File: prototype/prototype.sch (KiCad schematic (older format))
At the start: 2 parts

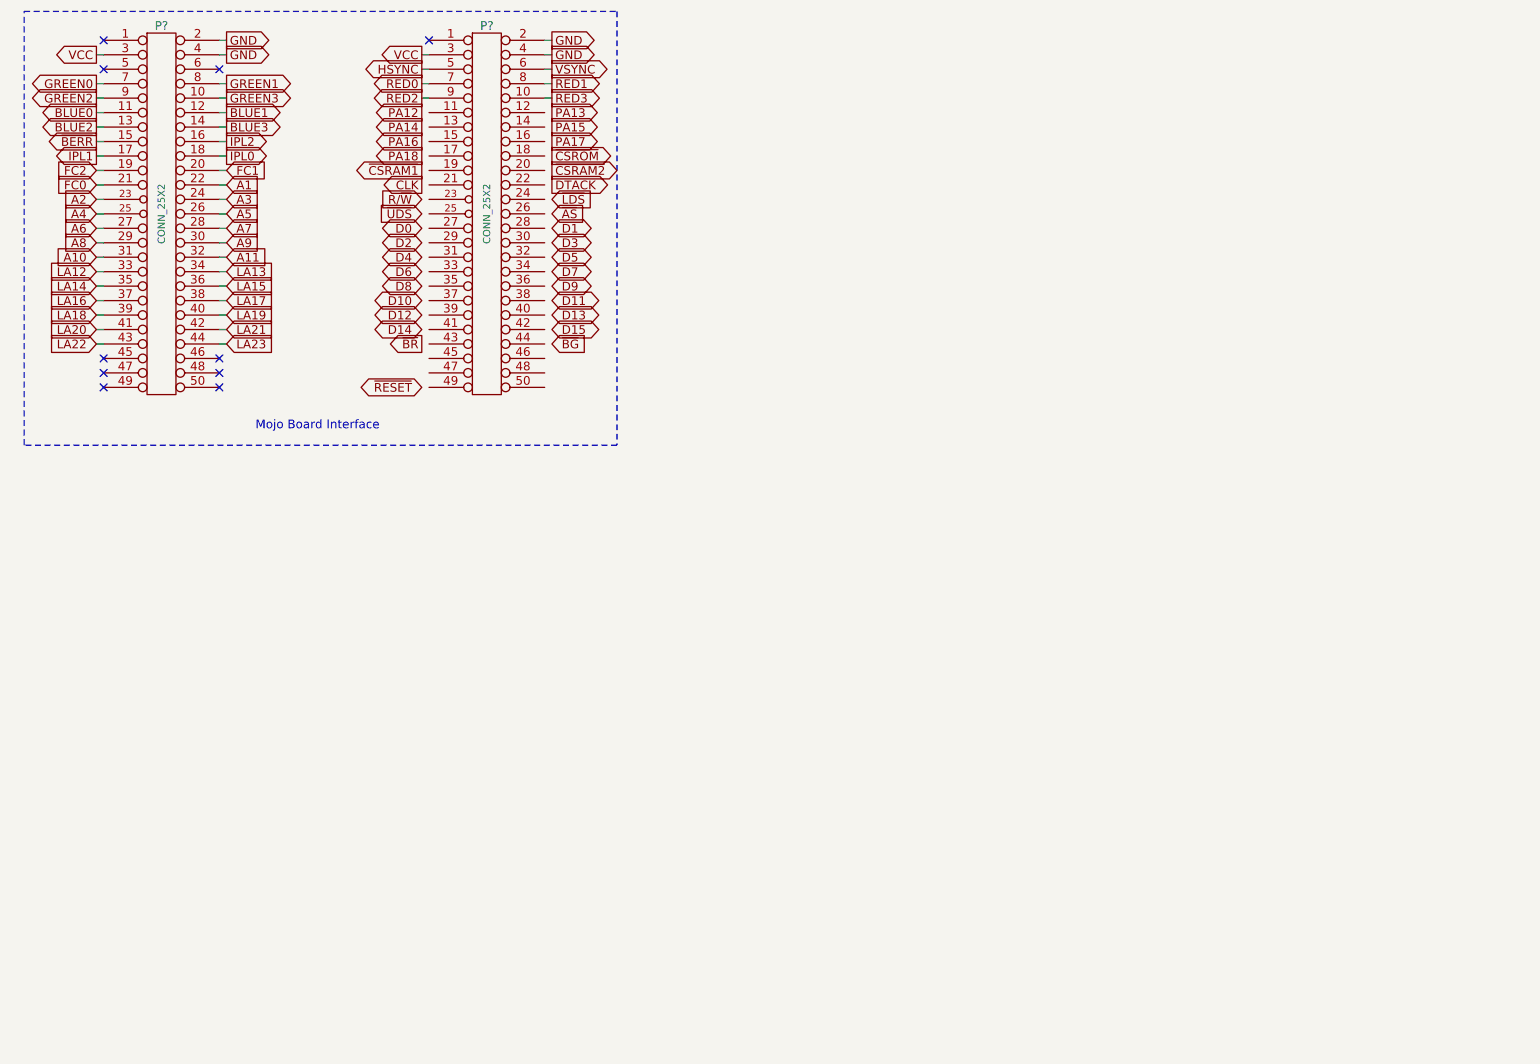
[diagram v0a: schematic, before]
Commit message: Wire up the MC68SEC000 chip in the prototype schematic.
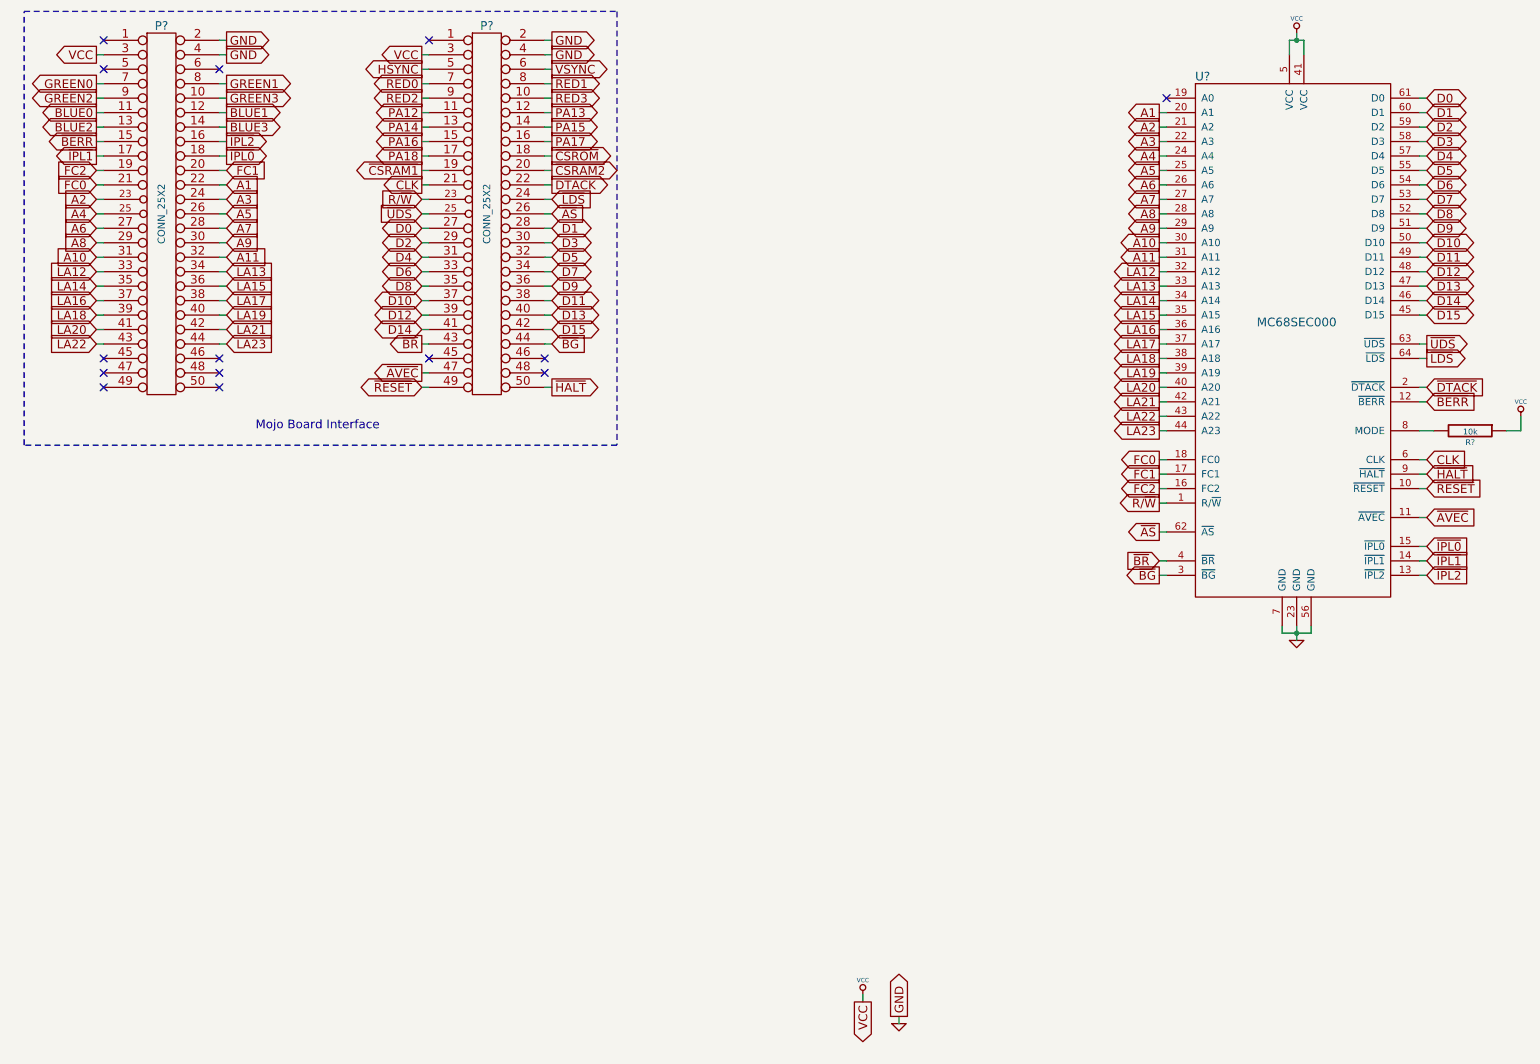
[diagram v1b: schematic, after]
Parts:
- added R?: 10k, symbol R
- added U?: MC68SEC000, symbol MC68SEC000
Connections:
- net A1: now also U?.20 (A1)
- net A10: now also U?.30 (A10)
- net A11: now also U?.31 (A11)
- net A2: now also U?.21 (A2)
- net A3: now also U?.22 (A3)
- net A4: now also U?.24 (A4)
- net A5: now also U?.25 (A5)
- net A6: now also U?.26 (A6)
- net A7: now also U?.27 (A7)
- net A8: now also U?.28 (A8)
- net A9: now also U?.29 (A9)
- net CLK: now also P?.21 (P21), U?.6 (CLK)
- net D0: now also P?.27 (P27), U?.61 (D0)
- net D1: now also P?.28 (P28), U?.60 (D1)
- net D10: now also P?.37 (P37), U?.50 (D10)
- net D11: now also P?.38 (P38), U?.49 (D11)
- net D12: now also P?.39 (P39), U?.48 (D12)
- net D13: now also P?.40 (P40), U?.47 (D13)
- net D14: now also P?.41 (P41), U?.46 (D14)
- net D15: now also P?.42 (P42), U?.45 (D15)
- net D2: now also P?.29 (P29), U?.59 (D2)
- net D3: now also P?.30 (P30), U?.58 (D3)
- net D4: now also P?.31 (P31), U?.57 (D4)
- net D5: now also P?.32 (P32), U?.55 (D5)
- net D6: now also P?.33 (P33), U?.54 (D6)
- net D7: now also P?.34 (P34), U?.53 (D7)
- net D8: now also P?.35 (P35), U?.52 (D8)
- net D9: now also P?.36 (P36), U?.51 (D9)
- net DTACK: now also P?.22 (P22)
- net FC0: now also U?.18 (FC0)
- net FC1: now also U?.17 (FC1)
- net FC2: now also U?.16 (FC2)
- net GND: now also U?.23 (GND), U?.56 (GND), U?.7 (GND)
- net LA12: now also U?.32 (A12)
- net LA13: now also U?.33 (A13)
- net LA14: now also U?.34 (A14)
- net LA15: now also U?.35 (A15)
- net LA16: now also U?.36 (A16)
- net LA17: now also U?.37 (A17)
- net LA18: now also U?.38 (A18)
- net LA19: now also U?.39 (A19)
- net LA20: now also U?.40 (A20)
- net LA21: now also U?.42 (A21)
- net LA22: now also U?.43 (A22)
- net LA23: now also U?.44 (A23)
- net PA12: now also P?.11 (P11)
- net PA13: now also P?.12 (P12)
- net PA14: now also P?.13 (P13)
- net PA15: now also P?.14 (P14)
- net PA16: now also P?.15 (P15)
- net PA17: now also P?.16 (P16)
- net PA18: now also P?.17 (P17)
- net R/~W: now also P?.23 (P23), U?.1 (R/~W)
- net VCC: now also R?.1, U?.41 (VCC), U?.5 (VCC)
- net ~AS: now also P?.26 (P26), U?.62 (~AS)
- net ~BERR: now also U?.12 (~BERR)
- net ~BG: now also P?.44 (P44), U?.3 (~BG)
- net ~BR: now also P?.43 (P43), U?.4 (~BR)
- net ~CSRAM1: now also P?.19 (P19)
- net ~CSRAM2: now also P?.20 (P20)
- net ~CSROM: now also P?.18 (P18)
- net ~LDS: now also P?.24 (P24), U?.64 (~LDS)
- net ~RESET: now also P?.49 (P49), U?.10 (~RESET)
- net ~UDS: now also P?.25 (P25), U?.63 (~UDS)
- net ~AVEC: now reaches P?.47 (P47)
- net ~AVEC: now also U?.11 (~AVEC)
- net ~HALT: now reaches P?.50 (P50)
- net ~HALT: now also U?.9 (~HALT)
- net IPL0 renamed ~IPL0
- net ~IPL0: now also U?.15 (~IPL0)
- net IPL1 renamed ~IPL1
- net ~IPL1: now also U?.14 (~IPL1)
- net IPL2 renamed ~IPL2
- net ~IPL2: now also U?.13 (~IPL2)
- new net: R?.2, U?.8 (MODE)
- new net ~DTACK: U?.2 (~DTACK)
- no-connect marks 10 -> 14

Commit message: Annotate the schematic components.
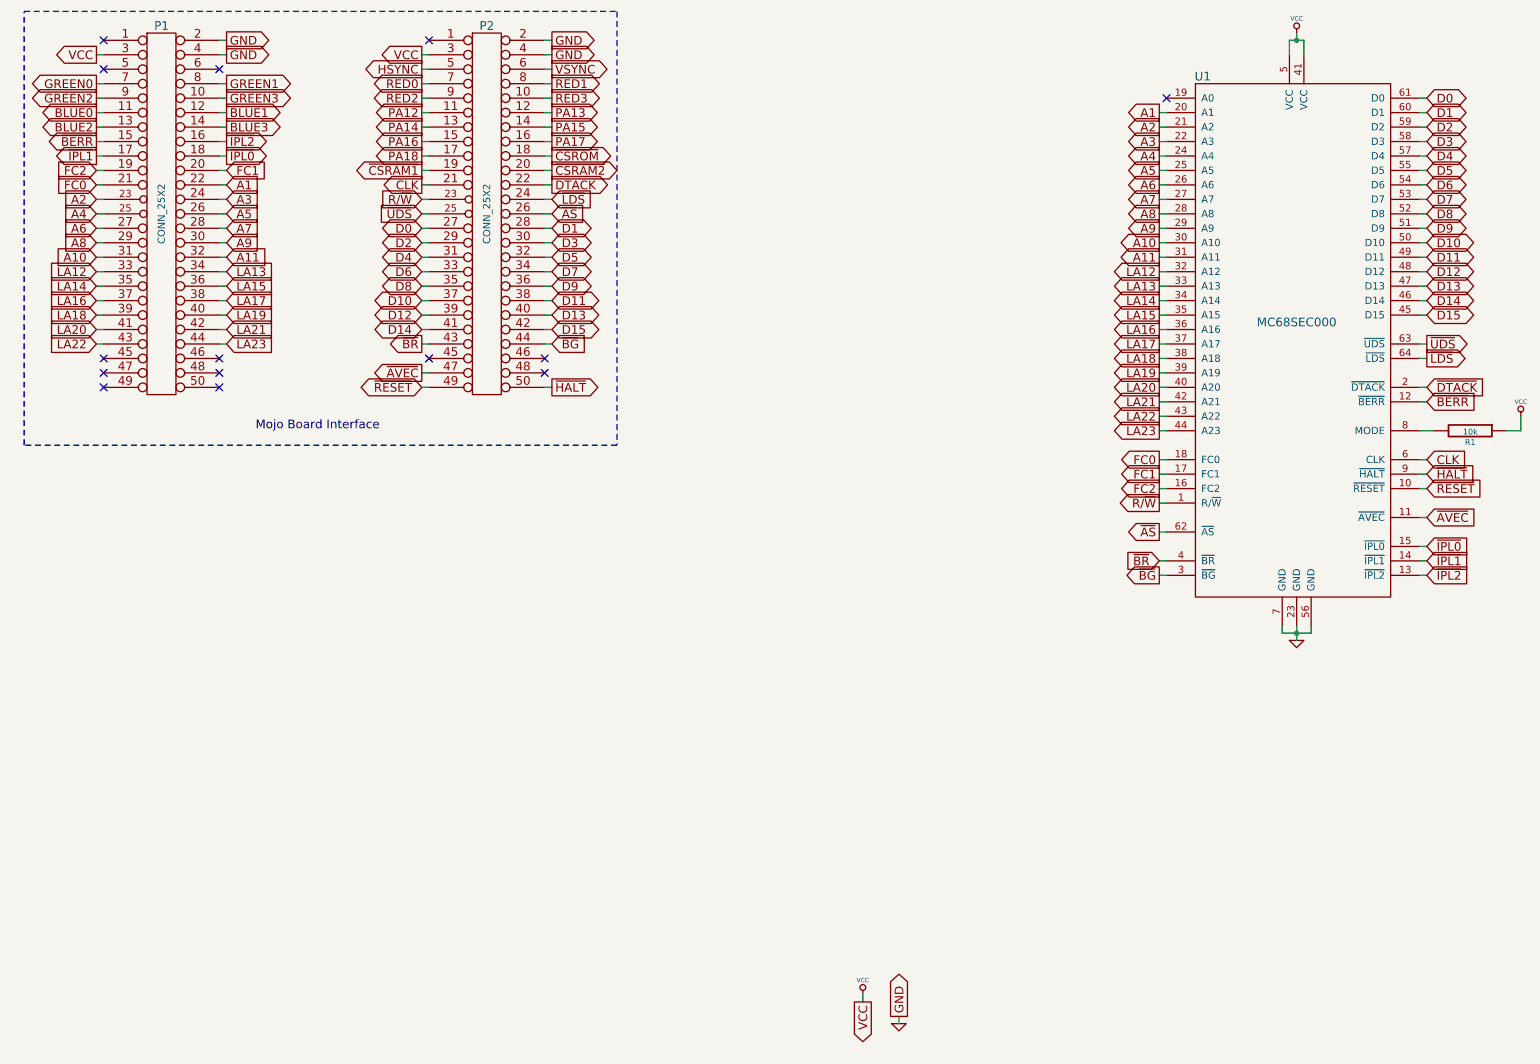
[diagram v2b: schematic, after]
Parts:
- gave numbers to parts that had none: 4
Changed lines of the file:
@@
 $EndDescr
 $Comp
-L CONN_25X2 P?
+L CONN_25X2 P1
 U 1 1 551890A6
 P 1550 2000
-F 0 "P?" H 1550 3300 60  0000 C CNN
+F 0 "P1" H 1550 3300 60  0000 C CNN
 F 1 "CONN_25X2" V 1550 2000 50  0000 C CNN
 F 2 "" H 1550 2000 60  0000 C CNN
@@
 $EndComp
 $Comp
-L CONN_25X2 P?
+L CONN_25X2 P2
 U 1 1 551890D2
 P 3800 2000
-F 0 "P?" H 3800 3300 60  0000 C CNN
+F 0 "P2" H 3800 3300 60  0000 C CNN
 F 1 "CONN_25X2" V 3800 2000 50  0000 C CNN
 F 2 "" H 3800 2000 60  0000 C CNN
@@
 	600  3600 600  600
 $Comp
-L MC68SEC000 U?
+L MC68SEC000 U1
 U 1 1 5518D2BF
 P 9400 2750
-F 0 "U?" H 8750 4450 60  0000 C CNN
+F 0 "U1" H 8750 4450 60  0000 C CNN
 F 1 "MC68SEC000" H 9400 2750 60  0000 C CNN
 F 2 "" H 9000 3800 60  0000 C CNN
@@
 	8450 4500 8500 4500
 $Comp
-L VCC #PWR?
+L VCC #PWR1
 U 1 1 5518ED2A
 P 6400 7400
-F 0 "#PWR?" H 6400 7500 30  0001 C CNN
+F 0 "#PWR1" H 6400 7500 30  0001 C CNN
 F 1 "VCC" H 6400 7500 30  0000 C CNN
 F 2 "" H 6400 7400 60  0000 C CNN
@@
 $EndComp
 $Comp
-L GND #PWR?
+L GND #PWR2
 U 1 1 5518ED53
 P 6650 7600
-F 0 "#PWR?" H 6650 7600 30  0001 C CNN
+F 0 "#PWR2" H 6650 7600 30  0001 C CNN
 F 1 "GND" H 6650 7530 30  0001 C CNN
 F 2 "" H 6650 7600 60  0000 C CNN
@@
 	6400 7400 6400 7450
 $Comp
-L VCC #PWR?
+L VCC #PWR3
 U 1 1 5518EEAA
 P 9400 750
-F 0 "#PWR?" H 9400 850 30  0001 C CNN
+F 0 "#PWR3" H 9400 850 30  0001 C CNN
 F 1 "VCC" H 9400 850 30  0000 C CNN
 F 2 "" H 9400 750 60  0000 C CNN
@@
 Connection ~ 9400 800
 $Comp
-L GND #PWR?
+L GND #PWR4
 U 1 1 5518EFE0
 P 9400 4950
-F 0 "#PWR?" H 9400 4950 30  0001 C CNN
+F 0 "#PWR4" H 9400 4950 30  0001 C CNN
 F 1 "GND" H 9400 4880 30  0001 C CNN
 F 2 "" H 9400 4950 60  0000 C CNN
@@
 	10250 4500 10300 4500
 $Comp
-L R R?
+L R R1
 U 1 1 55190758
 P 10600 3500
-F 0 "R?" V 10680 3500 40  0000 C CNN
+F 0 "R1" V 10680 3500 40  0000 C CNN
 F 1 "10k" V 10607 3501 40  0000 C CNN
 F 2 "" V 10530 3500 30  0000 C CNN
@@
 	10250 3500 10350 3500
 $Comp
-L VCC #PWR?
+L VCC #PWR5
 U 1 1 55190866
 P 10950 3400
-F 0 "#PWR?" H 10950 3500 30  0001 C CNN
+F 0 "#PWR5" H 10950 3500 30  0001 C CNN
 F 1 "VCC" H 10950 3500 30  0000 C CNN
 F 2 "" H 10950 3400 60  0000 C CNN

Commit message: Decoupling caps for MC68SEC000.
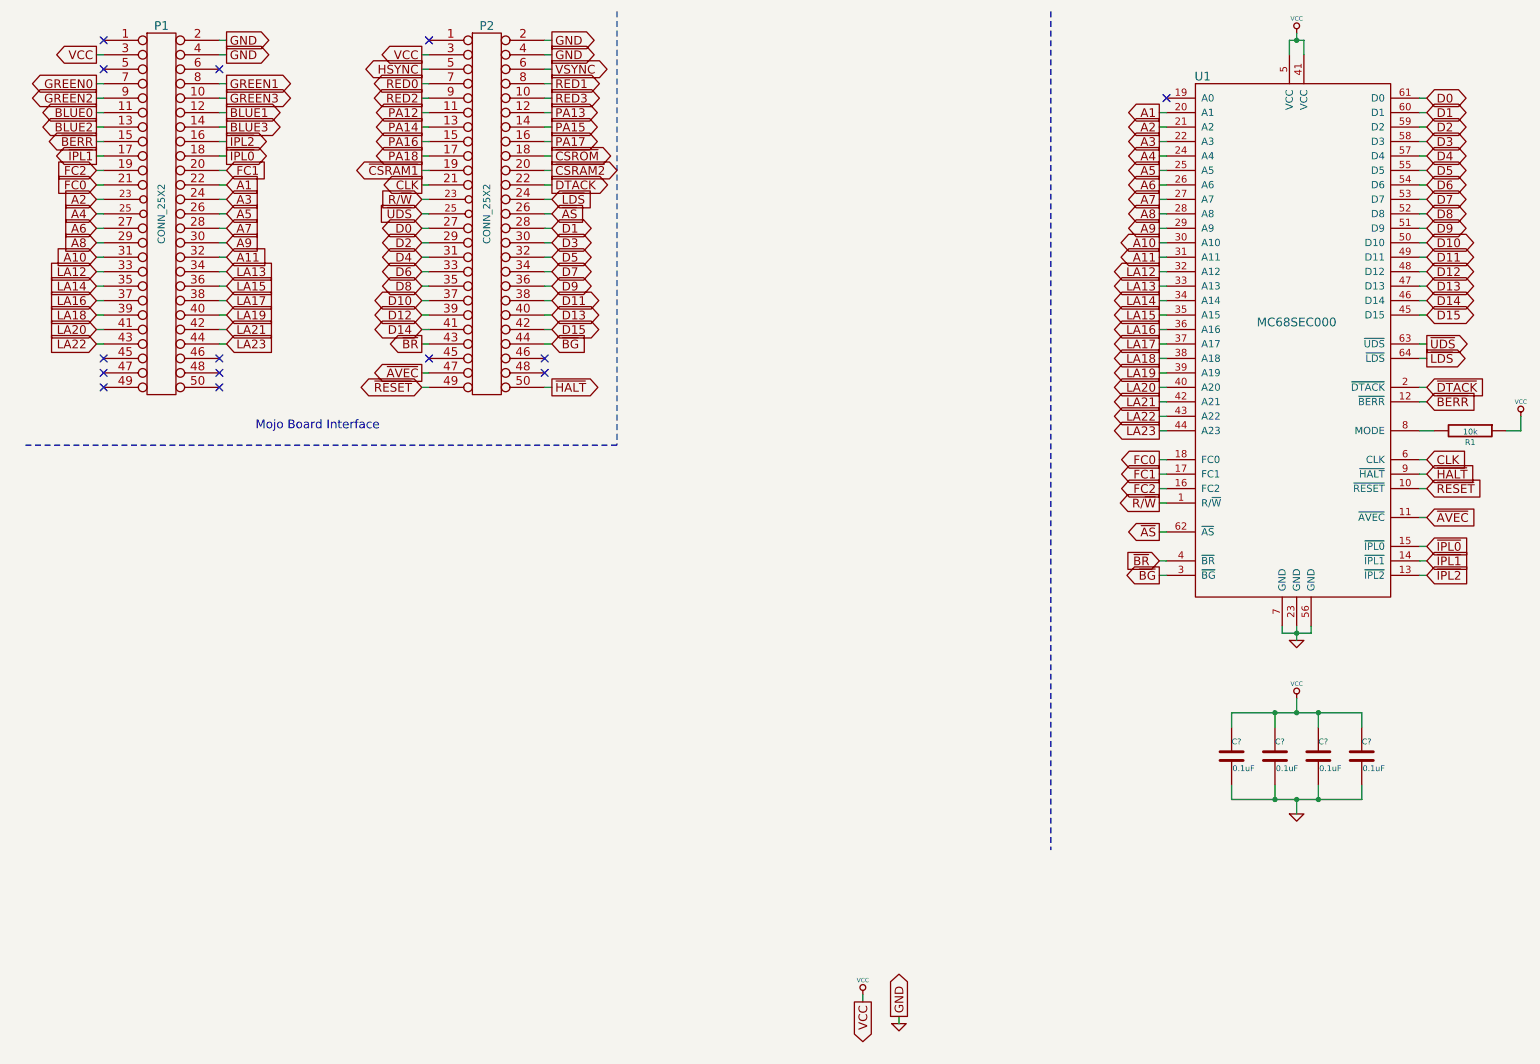
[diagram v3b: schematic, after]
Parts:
- added C? (x4): 0.1uF, symbol C
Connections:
- net GND: now also C?.2, C?.2, C?.2, C?.2
- net VCC: now also C?.1, C?.1, C?.1, C?.1
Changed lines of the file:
@@
 Mojo Board Interface
-Wire Notes Line
-	600  600  4700 600
 Wire Notes Line
 	4700 600  4700 3600
 Wire Notes Line
 	4700 3600 600  3600
-Wire Notes Line
-	600  3600 600  600
 $Comp
 L MC68SEC000 U1
@@
 Wire Wire Line
 	10950 3500 10950 3400
+$Comp
+L C C?
+U 1 1 5519107D
+P 9250 5750
+F 0 "C?" H 9250 5850 40  0000 L CNN
+F 1 "0.1uF" H 9256 5665 40  0000 L CNN
+F 2 "" H 9288 5600 30  0000 C CNN
+F 3 "" H 9250 5750 60  0000 C CNN
+	1    9250 5750
+	1    0    0    -1
+$EndComp
+$Comp
+L C C?
+U 1 1 551910BD
+P 9550 5750
+F 0 "C?" H 9550 5850 40  0000 L CNN
+F 1 "0.1uF" H 9556 5665 40  0000 L CNN
+F 2 "" H 9588 5600 30  0000 C CNN
+F 3 "" H 9550 5750 60  0000 C CNN
+	1    9550 5750
+	1    0    0    -1
+$EndComp
+$Comp
+L C C?
+U 1 1 55191170
+P 9850 5750
+F 0 "C?" H 9850 5850 40  0000 L CNN
+F 1 "0.1uF" H 9856 5665 40  0000 L CNN
+F 2 "" H 9888 5600 30  0000 C CNN
+F 3 "" H 9850 5750 60  0000 C CNN
+	1    9850 5750
+	1    0    0    -1
+$EndComp
+$Comp
+L C C?
+U 1 1 5519119C
+P 8950 5750
+F 0 "C?" H 8950 5850 40  0000 L CNN
+F 1 "0.1uF" H 8956 5665 40  0000 L CNN
+F 2 "" H 8988 5600 30  0000 C CNN
+F 3 "" H 8950 5750 60  0000 C CNN
+	1    8950 5750
+	1    0    0    -1
+$EndComp
+$Comp
+L VCC #PWR?
+U 1 1 551911CA
+P 9400 5350
+F 0 "#PWR?" H 9400 5450 30  0001 C CNN
+F 1 "VCC" H 9400 5450 30  0000 C CNN
+F 2 "" H 9400 5350 60  0000 C CNN
+F 3 "" H 9400 5350 60  0000 C CNN
+	1    9400 5350
+	1    0    0    -1
+$EndComp
+$Comp
+L GND #PWR?
+U 1 1 551911E5
+P 9400 6150
+F 0 "#PWR?" H 9400 6150 30  0001 C CNN
+F 1 "GND" H 9400 6080 30  0001 C CNN
+F 2 "" H 9400 6150 60  0000 C CNN
+F 3 "" H 9400 6150 60  0000 C CNN
+	1    9400 6150
+	1    0    0    -1
+$EndComp
+Wire Wire Line
+	9400 5450 9400 5350
+Wire Wire Line
+	8950 5450 9850 5450
+Wire Wire Line
+	9250 5450 9250 5550
+Wire Wire Line
+	8950 5450 8950 5550
+Connection ~ 9250 5450
+Wire Wire Line
+	9550 5450 9550 5550
+Connection ~ 9400 5450
+Wire Wire Line
+	9850 5450 9850 5550
+Connection ~ 9550 5450
+Wire Wire Line
+	9400 6150 9400 6050
+Wire Wire Line
+	8950 6050 9850 6050
+Wire Wire Line
+	8950 6050 8950 5950
+Wire Wire Line
+	9250 6050 9250 5950
+Connection ~ 9250 6050
+Wire Wire Line
+	9550 6050 9550 5950
+Connection ~ 9400 6050
+Wire Wire Line
+	9850 6050 9850 5950
+Connection ~ 9550 6050
+Wire Notes Line
+	7700 600  7700 6400
 $EndSCHEMATC
